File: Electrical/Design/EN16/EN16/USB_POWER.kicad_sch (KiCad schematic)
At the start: 34 parts, among them J1 USB_C_TYPE-C-32-M-12, U15 FUSB302BMPX (NF), U16 FUSB302BMPX (NF), U17 MT9700, U4 SESRV05-4, U5 LN1134A332MR-G, U6 LN1134A332MR-G

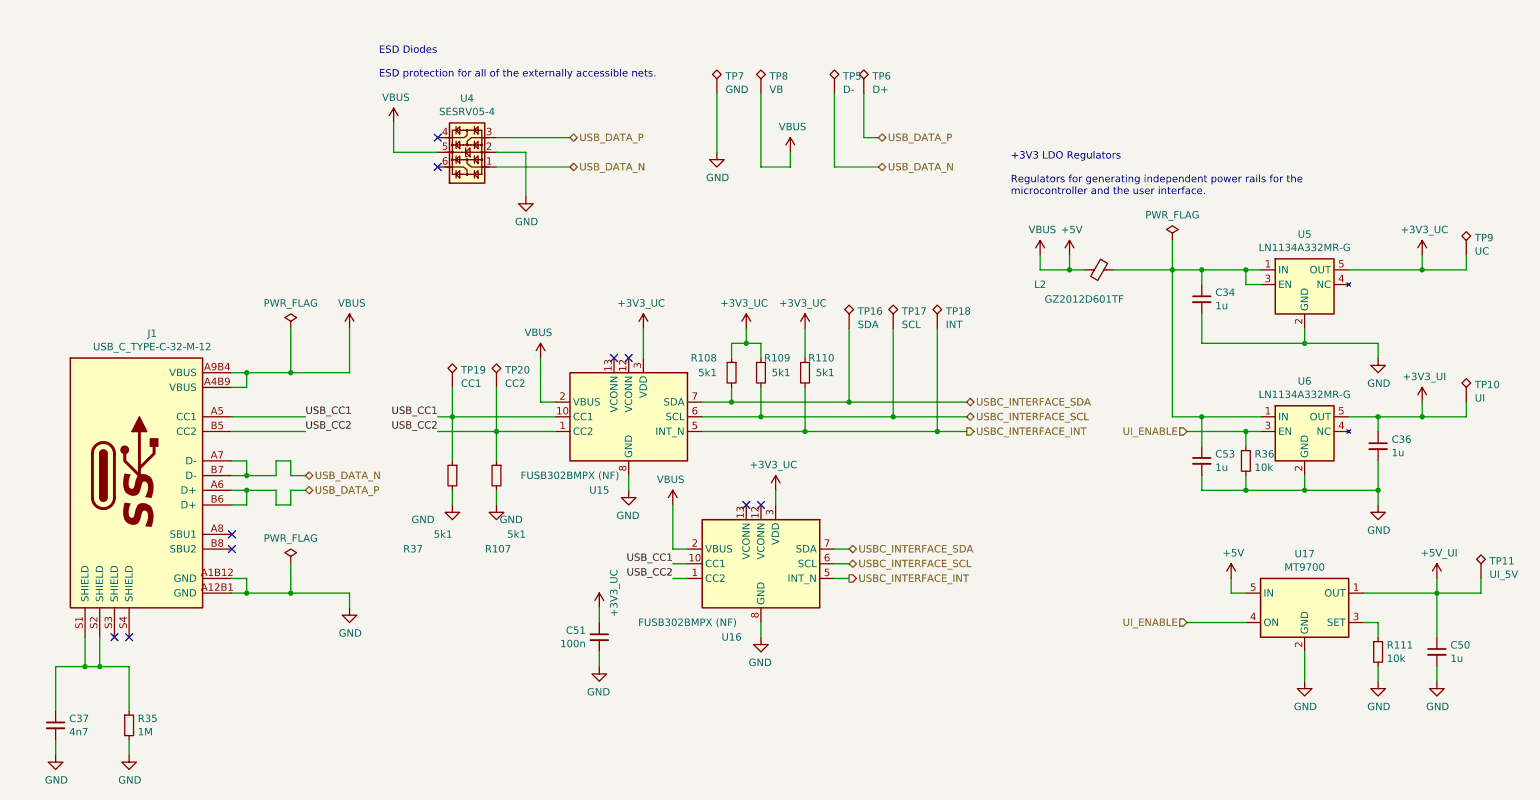
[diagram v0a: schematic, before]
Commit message: SUKU EN16 ki7 project cloned from PO16_BU16 base project
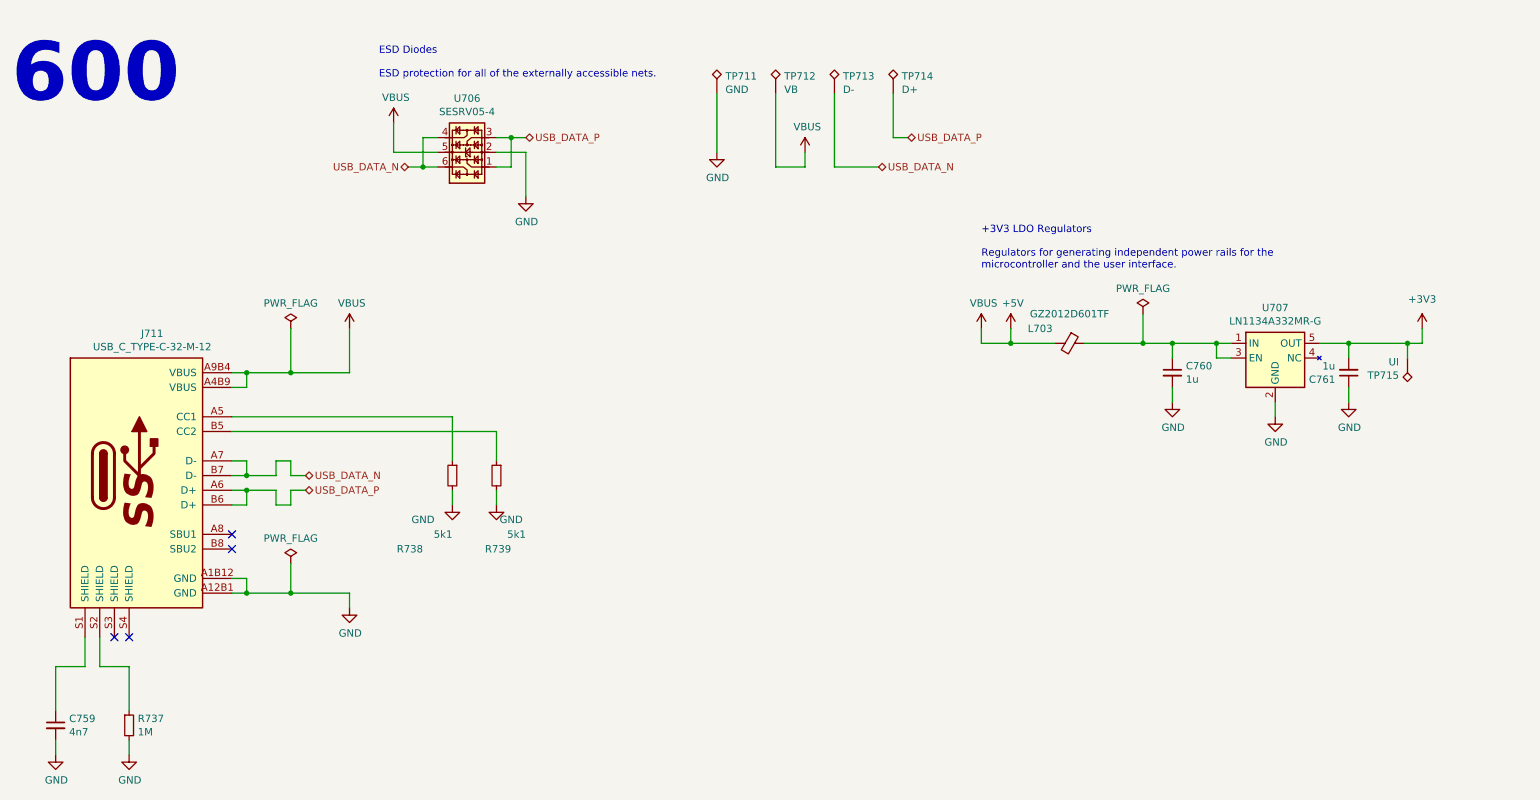
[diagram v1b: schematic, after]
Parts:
- removed C50, C53: 1u, suku_basics:CAP_0805, symbol suku_basics:CAP
- removed C51: 100n, suku_basics:CAP_0805, symbol suku_basics:CAP
- removed R108, R109, R110: 5k1, suku_basics:RES_0805, symbol suku_basics:RES
- removed R111, R36: 10k, suku_basics:RES_0805, symbol suku_basics:RES
- removed TP11: UI_5V, TestPoint:TestPoint_Pad_D1.0mm, symbol Connector:TestPoint_Alt
- removed TP16: SDA, TestPoint:TestPoint_Pad_D1.0mm, symbol Connector:TestPoint_Alt
- removed TP17: SCL, TestPoint:TestPoint_Pad_D1.0mm, symbol Connector:TestPoint_Alt
- removed TP18: INT, TestPoint:TestPoint_Pad_D1.0mm, symbol Connector:TestPoint_Alt
- removed TP19: CC1, TestPoint:TestPoint_Pad_D1.0mm, symbol Connector:TestPoint_Alt
- removed TP20: CC2, TestPoint:TestPoint_Pad_D1.0mm, symbol Connector:TestPoint_Alt
- removed TP9: UC, TestPoint:TestPoint_Pad_D1.0mm, symbol Connector:TestPoint_Alt
- removed U15, U16: FUSB302BMPX (NF), Package_DFN_QFN:WQFN-14-1EP_2.5x2.5mm_P0.5mm_EP1.45x1.45mm, symbol Interface_USB:FUSB302BMPX
- removed U17: MT9700, suku_basics:SOT-23-5, symbol suku_basics:PMIC_MT9700
- removed U6: LN1134A332MR-G, suku_basics:SOT-23-5, symbol suku_basics:U_REGULATOR_SOT23-5
- C759: renamed from C37; footprint suku_basics:CAP_0805 -> suku_basics:CAP_0402
- C760: renamed from C34; footprint suku_basics:CAP_0805 -> suku_basics:CAP_0402
- C761: renamed from C36; footprint suku_basics:CAP_0805 -> suku_basics:CAP_0402
- R737: renamed from R35; footprint suku_basics:RES_0805 -> suku_basics:RES_0402
- R738: renamed from R37; footprint suku_basics:RES_0805 -> suku_basics:RES_0402
- R739: renamed from R107; footprint suku_basics:RES_0805 -> suku_basics:RES_0402
- TP711: renamed from TP7; footprint TestPoint:TestPoint_Pad_D1.0mm -> TestPoint:TestPoint_Pad_1.0x1.0mm
- renumbered J1 to J711, L2 to L703, TP8 to TP712, TP5 to TP713, TP6 to TP714, TP10 to TP715, U4 to U706, U5 to U707
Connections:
- net GND: now also C761.1; no longer C761.2
- net USB_DATA_N: now also U706.4, U706.6; no longer U706.1
- net USB_DATA_P: now also U706.1
- net at C759.1, J711.S1 (SHIELD): no longer J711.S2 (SHIELD), R737.1
- net +3V3_UC renamed +3V3
- net +3V3: now also C761.2, TP715.1
- removed net +3V3_UI: C761.1, TP715.1
- net USB_CC1: no longer names the net of J711.A5 (CC1), R738.1
- net USB_CC2: no longer names the net of J711.B5 (CC2), R739.1
- new net: J711.S2 (SHIELD), R737.1
- no-connect marks 10 -> 4
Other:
- note added: "600"
- moved on the sheet: C760, C761, L703, TP712, TP714, TP715, U707
